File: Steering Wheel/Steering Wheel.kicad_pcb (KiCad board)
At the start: 2 copper layers, 28 parts, among them J1 DTF13-4P, J2 Upshift Paddle, J3 Downshift Paddle, J4 Neutral Button, J5 Start Button, J6 Unused Button 1, J7 Unused Button 2, J8 Selection Knob, U1 AS1115-BSST, U2 CC56-12GWA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

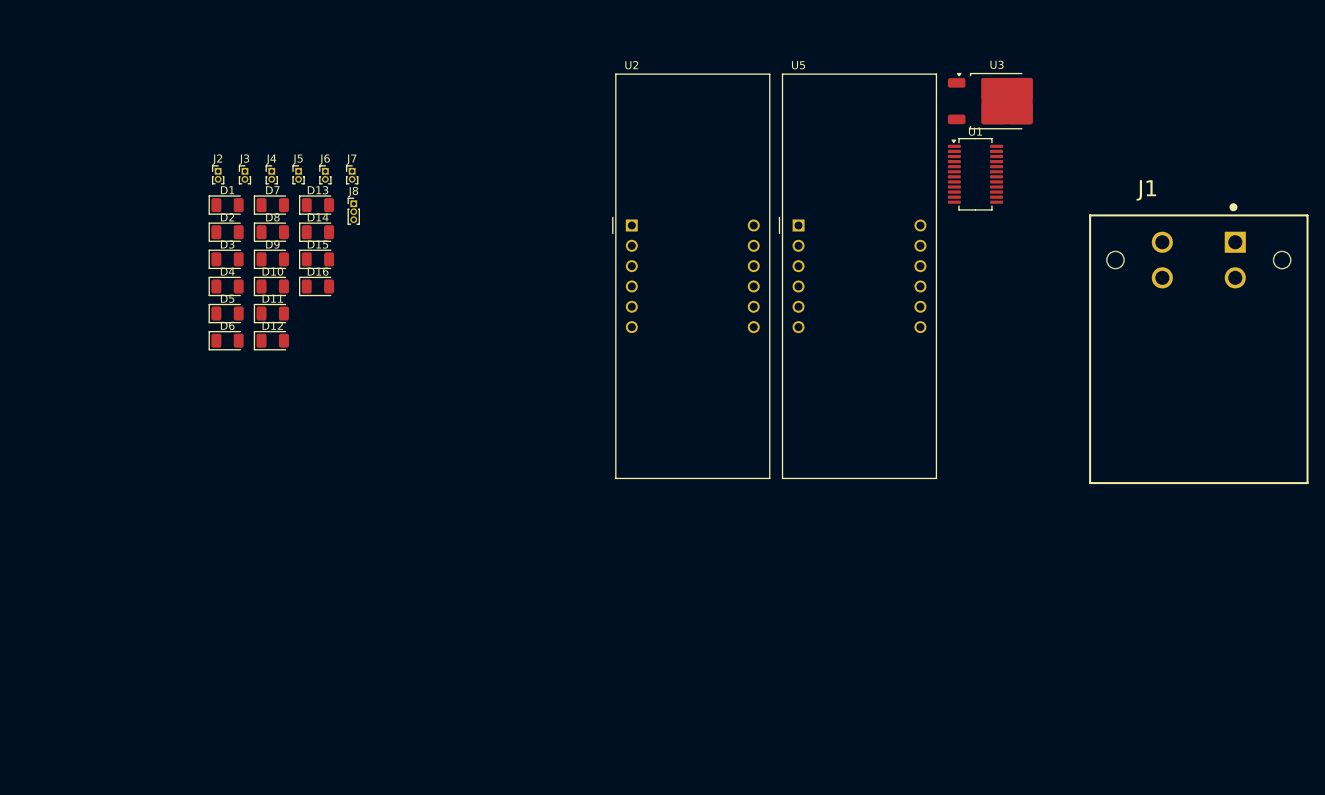
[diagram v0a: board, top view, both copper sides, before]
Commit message: feat: begin SCU, RLM, PCU, ETC. update SWU
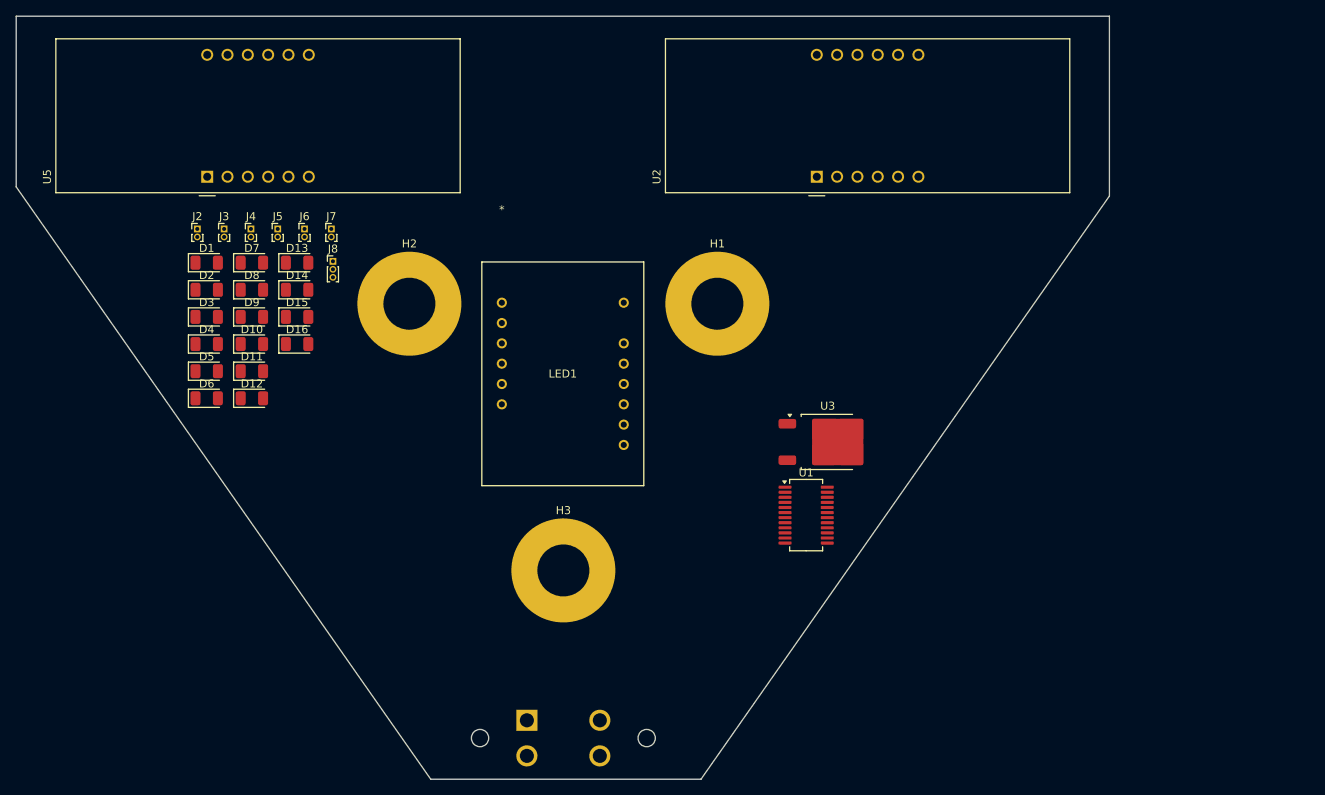
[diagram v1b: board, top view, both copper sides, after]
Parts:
- added H1: MountingHole_Pad, MountingHole:MountingHole_6.5mm_Pad, F.Cu at (141.0, 87.8)
- added H2: MountingHole_Pad, MountingHole:MountingHole_6.5mm_Pad, F.Cu at (102.5, 87.8)
- added H3: MountingHole_Pad, MountingHole:MountingHole_6.5mm_Pad, F.Cu at (121.7, 121.1)
- added LED1: LDS-C814RI, LDS_C814RI:LDS-C814RI_LUM, F.Cu at (114.0, 87.6)
- J1: moved to B.Cu
- moved J1 99.4 mm to (121.7, 142.0), turned to 180 degrees
- moved U5 74.2 mm to (77.2, 71.9), turned to 90 degrees
- moved U1 47.6 mm to (152.1, 114.2)
- moved U3 47.6 mm to (154.8, 105.0)
- moved U2 23.9 mm to (153.4, 71.9), turned to 90 degrees
- moved D1 7.66 mm to (77.2, 82.6)
- moved D10 7.66 mm to (82.8, 92.8)
- moved D11 7.66 mm to (82.8, 96.2)
- moved D12 7.66 mm to (82.8, 99.6)
- moved D13 7.66 mm to (88.5, 82.6)
- moved D14 7.66 mm to (88.5, 86.0)
- moved D15 7.66 mm to (88.5, 89.4)
- moved D16 7.66 mm to (88.5, 92.8)
- moved D2 7.66 mm to (77.2, 86.0)
- moved D3 7.66 mm to (77.2, 89.4)
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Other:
- board outline added: 136.7 x 95.4 mm
